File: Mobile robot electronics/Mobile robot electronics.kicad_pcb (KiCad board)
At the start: 2 copper layers, 41 parts, among them J1 Front_Sens, J10 Conn_01x06_Male, J2 Back_Sens, J3 Left_Sens, J4 Right_sens, J5 Conn_01x02_Male, J6 Conn_01x02_Male, J7 Conn_01x06_Male, J8 Conn_01x06_Male, J9 Conn_01x06_Male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

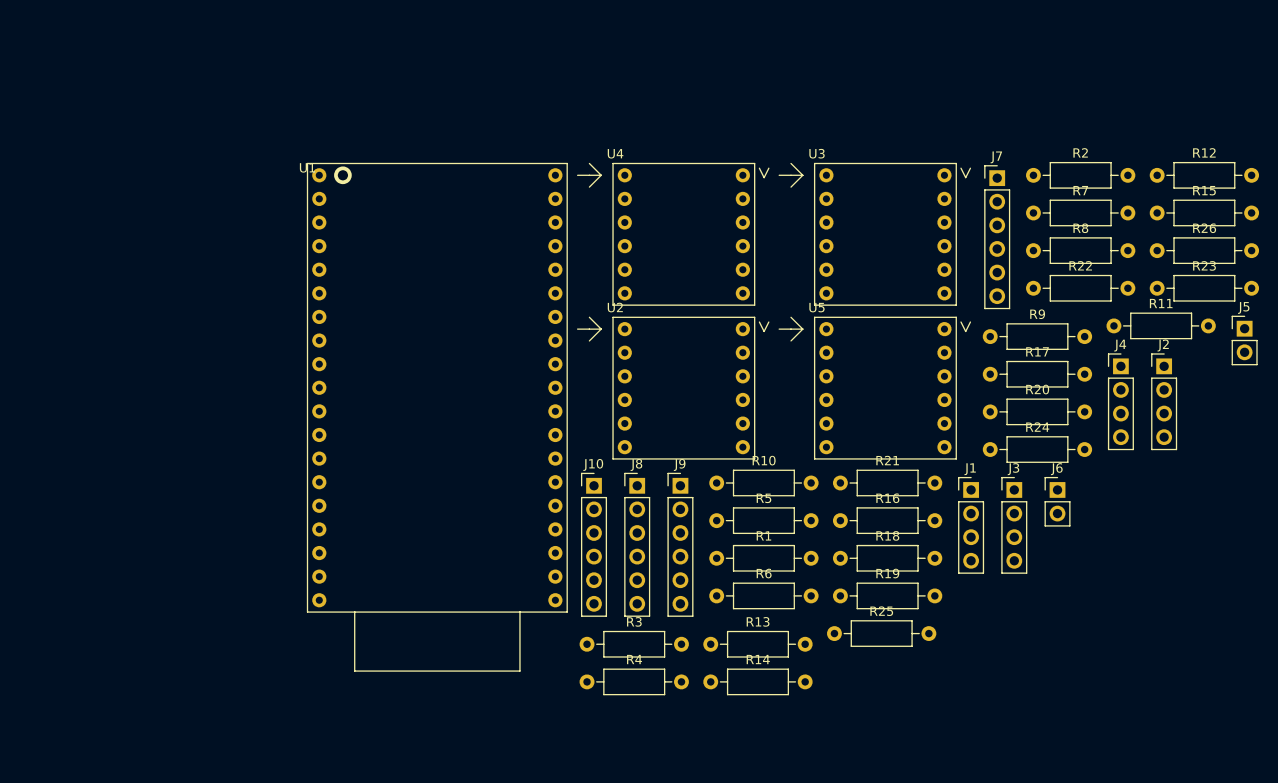
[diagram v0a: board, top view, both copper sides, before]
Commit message: routed tracks for pcb, changed some pins on esp
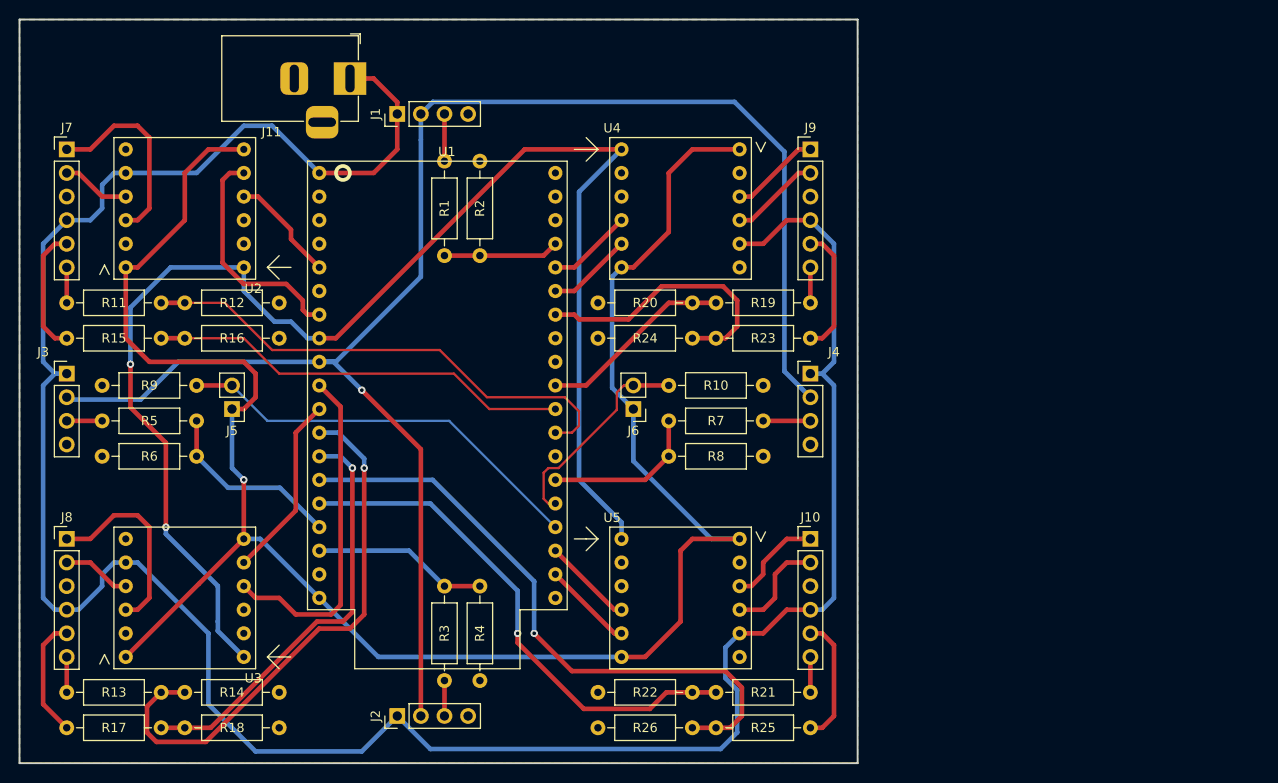
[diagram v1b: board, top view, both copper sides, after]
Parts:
- added J11: Conn_01x03, Connector_BarrelJack:BarrelJack_Horizontal, F.Cu at (68.6, 41.9)
- moved R15 118.1 mm to (38.1, 69.8)
- moved R11 112.7 mm to (38.1, 66.0)
- moved J5 109.3 mm to (55.9, 77.5), turned to 180 degrees
- moved R17 106.4 mm to (38.1, 111.8)
- moved R12 105.5 mm to (50.8, 66.0)
- moved J3 102.7 mm to (38.1, 73.7)
- moved J7 100.2 mm to (38.1, 49.5)
- moved J2 90.7 mm to (73.7, 110.5), turned to 90 degrees
- moved R9 85.6 mm to (52.1, 74.9), turned to 180 degrees
- moved U3 81.1 mm to (58.4, 105.4), turned to 180 degrees
- moved J1 73.8 mm to (73.7, 45.7), turned to 90 degrees
- moved R16 73.2 mm to (50.8, 69.8)
- moved R18 72.9 mm to (50.8, 111.8)
- moved R26 71.7 mm to (105.4, 111.8), turned to 180 degrees
- moved R13 69.5 mm to (38.1, 108.0)
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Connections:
- J4 pad 1: Net-(J4-Pad1) -> +5V
- U1 pad 12: Motor_FR_PWM -> Encoder_3_B
- U1 pad 13: Motor_FR_DIR -> Encoder_3_A
- U1 pad 16: Front_US -> Left_US
- U1 pad 23: Left_US -> Front_US
- U1 pad 24: Encoder_3_A -> Motor_FR_PWM
- U1 pad 25: Encoder_3_B -> Motor_FR_DIR
- U1 pad 36: TRIG_US -> Motor_BR_PWM
- U1 pad 37: Motor_EN -> Motor_BR_DIR
- U1 pad 8: Motor_BR_PWM -> Motor_EN
- U1 pad 9: Motor_BR_DIR -> TRIG_US
- U2 pad 4: (no net) -> Motor_FL_PWM
- U3 pad 4: (no net) -> Motor_BL_PWM
- U4 pad 4: (no net) -> Motor_FR_PWM
- U5 pad 4: (no net) -> Motor_BR_PWM
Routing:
- net +5V: track 0.00 -> 270.6 mm
- net +3V3: track 0.00 -> 209.3 mm, vias 0 -> 1
- net TRIG_US: track 0.00 -> 174.2 mm, vias 0 -> 1
- net Motor_EN: track 0.00 -> 156.0 mm, vias 0 -> 2
- net Encoder_4_A: track 0.00 -> 66.9 mm, vias 0 -> 1
- net Encoder_3_B: track 0.00 -> 59.7 mm, vias 0 -> 1
- net Encoder_4_B: track 0.00 -> 55.8 mm, vias 0 -> 1
- net Encoder_1_B: track 0.00 -> 54.2 mm
- net Encoder_1_A: track 0.00 -> 45.6 mm
- net Encoder_3_A: track 0.00 -> 45.3 mm, vias 0 -> 1
- net Load_SW2: track 0.00 -> 44.9 mm
- net Motor_BL_PWM: track 0.00 -> 36.7 mm
- net Encoder_2_A: track 0.00 -> 30.0 mm
- net Motor_FL_DIR: track 0.00 -> 24.8 mm
- net Load_SW1: track 0.00 -> 22.7 mm
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- added copper zone on B.Cu, net GND
- added copper zone on F.Cu, net GND
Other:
- board outline added: 90.2 x 80 mm
- rule trace_min: 0.2 -> 0.127
- rule via_min_drill: 0.3 -> 0.2

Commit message: added mounting holes for PCB
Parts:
- added H1: MountingHole, MountingHole:MountingHole_4.3mm_M4, F.Cu at (112.4, 41.9)
- added H2: MountingHole, MountingHole:MountingHole_4.3mm_M4, F.Cu at (43.2, 41.9)
- added H3: MountingHole, MountingHole:MountingHole_4.3mm_M4, F.Cu at (66.7, 109.9)
- moved R1 1.27 mm to (78.7, 52.1)
- moved R2 1.27 mm to (82.5, 62.2)
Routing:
- net Net-(J1-Pad3): track 5.08 -> 6.35 mm
- net Front_US: track 12.5 -> 13.0 mm

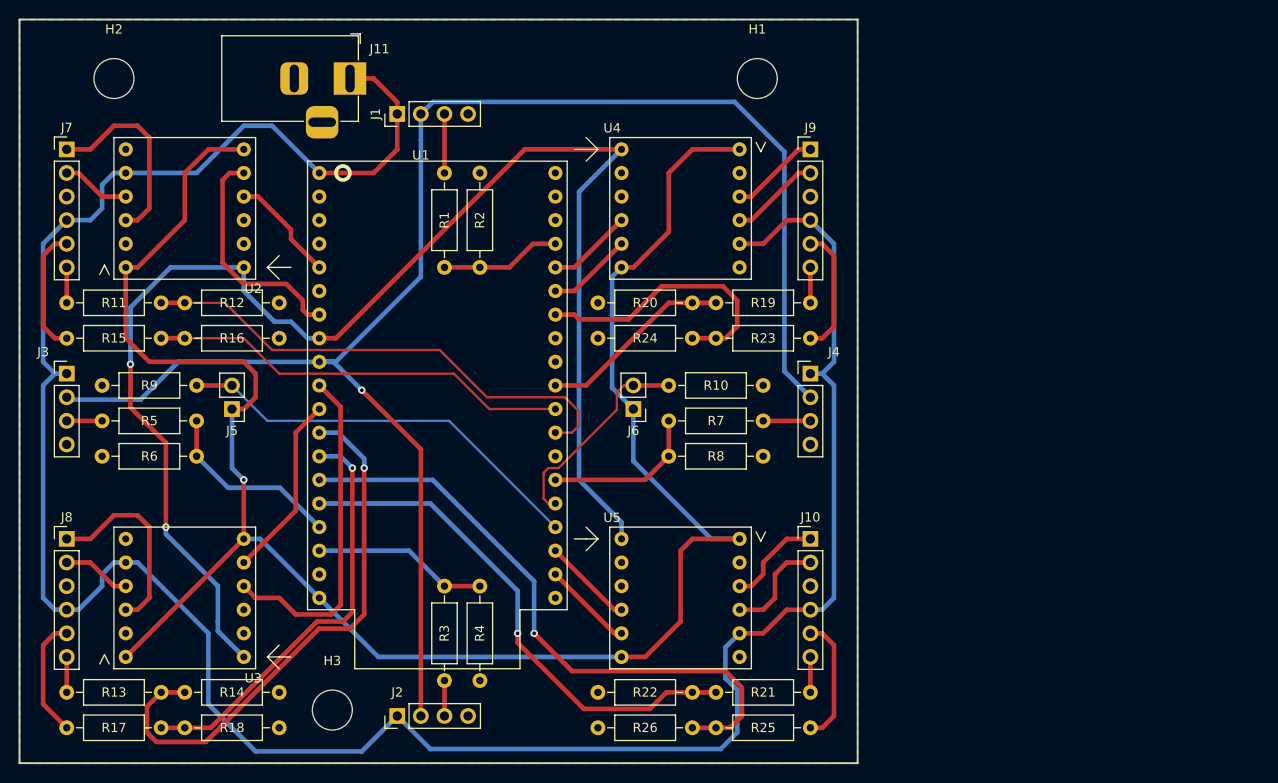
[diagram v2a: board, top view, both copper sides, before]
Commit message: made motor traces thicker, added silk screen stuff
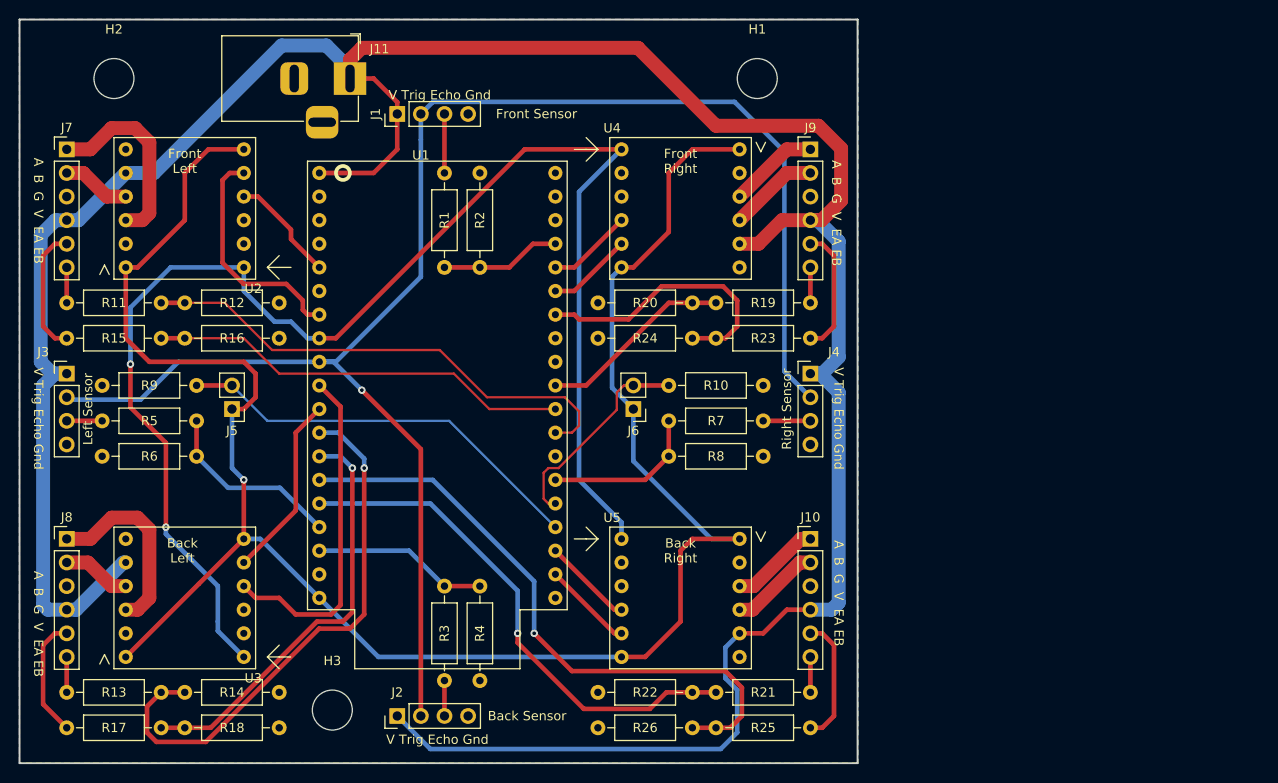
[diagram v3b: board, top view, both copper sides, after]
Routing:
- net +5V: track 270.6 -> 307.0 mm
- net MotorBRB: track 11.2 -> 9.72 mm
- net MotorBRA: track 10.5 -> 9.72 mm
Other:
- board text added: "A B G V EA EB"
- board text added: "Back Left"
- board text added: "Back Right"
- board text added: "Back Sensor"
- board text added: "Front Left"
- board text added: "Front Right"
- board text added: "Front Sensor"
- board text added: "Left Sensor"
- board text added: "Right Sensor"
- board text added: "V Trig Echo Gnd"
